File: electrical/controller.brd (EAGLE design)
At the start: 101.6 x 25.4 mm, 34 parts, among them IC1 MCP6232, IC2 LTC1661MSOP8, IC3 MCP6232, IC4 ICM7555, IC5 CD40109B, Q1 DMP3098, Q3 600mA/40V, U1 U3V16F15, U2 U3V16F15

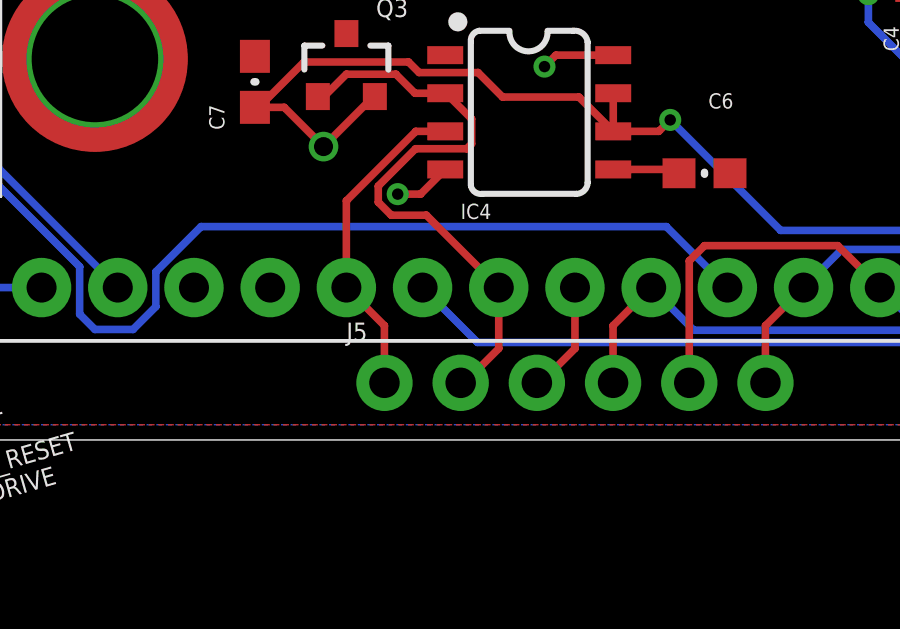
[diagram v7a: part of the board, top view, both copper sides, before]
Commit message: Some pin renaming to make things easier to understand...
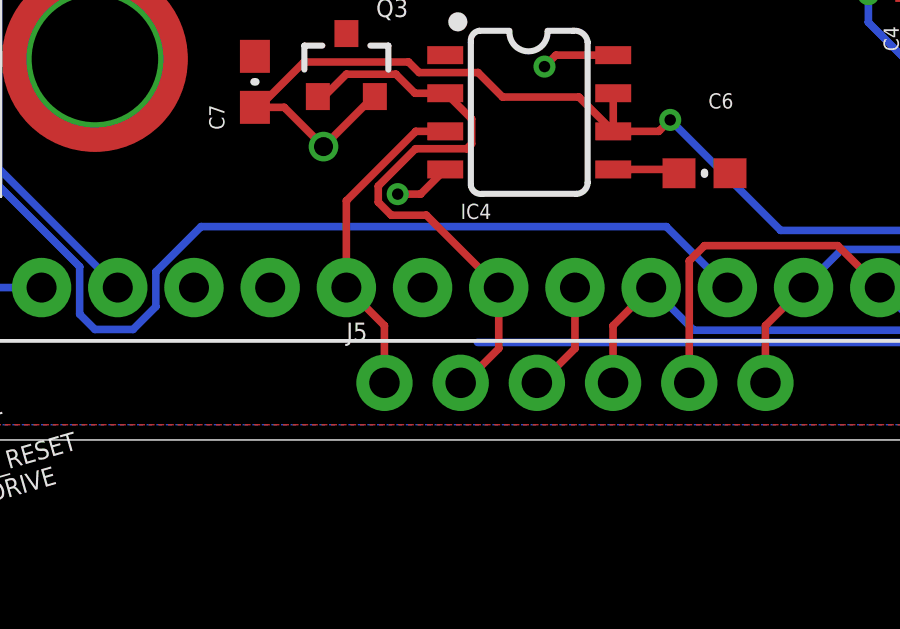
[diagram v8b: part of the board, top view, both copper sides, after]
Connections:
- net WAKE renamed BEMF_WAKE
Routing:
- net BEMF_WAKE: track 41.7 -> 39.1 mm
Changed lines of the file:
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@@
 <wire x1="60.10648125" y1="7.54651875" x2="60.10648125" y2="7.5644" width="0.254" layer="1"/>
-</signal>
-<signal name="WAKE">
-<contactref element="IC1" pad="7"/>
-<contactref element="UC1" pad="3"/>
-<wire x1="52.01" y1="6.985" x2="53.9082625" y2="6.985" width="0.254" layer="1"/>
-<wire x1="61.087" y1="1.905" x2="58.293" y2="4.699" width="0.254" layer="1"/>
-<wire x1="58.293" y1="4.699" x2="56.1942625" y2="4.699" width="0.254" layer="1"/>
-<wire x1="56.1942625" y1="4.699" x2="53.9082625" y2="6.985" width="0.254" layer="1"/>
-<contactref element="J4" pad="3"/>
-<wire x1="61.087" y1="1.905" x2="59.7408" y2="3.2512" width="0.254" layer="16"/>
-<wire x1="33.7058" y1="3.2512" x2="31.877" y2="5.08" width="0.254" layer="16"/>
-<wire x1="59.7408" y1="3.2512" x2="33.7058" y2="3.2512" width="0.254" layer="16"/>
 </signal>
 <signal name="DRIVE">
@@
 <wire x1="62.897" y1="9.798" x2="62.897" y2="10.598" width="0.254" layer="1"/>
 </signal>
+<signal name="BEMF_WAKE">
+<contactref element="UC1" pad="3"/>
+<contactref element="IC1" pad="7"/>
+<wire x1="52.01" y1="6.985" x2="53.9082625" y2="6.985" width="0.254" layer="1"/>
+<wire x1="61.087" y1="1.905" x2="58.293" y2="4.699" width="0.254" layer="1"/>
+<wire x1="58.293" y1="4.699" x2="56.1942625" y2="4.699" width="0.254" layer="1"/>
+<wire x1="56.1942625" y1="4.699" x2="53.9082625" y2="6.985" width="0.254" layer="1"/>
+<contactref element="J4" pad="3"/>
+<wire x1="61.087" y1="1.905" x2="59.7408" y2="3.2512" width="0.254" layer="16"/>
+<wire x1="59.7408" y1="3.2512" x2="33.7058" y2="3.2512" width="0.254" layer="16"/>
+<wire x1="33.7058" y1="3.2512" x2="31.877" y2="5.08" width="0" layer="19" extent="16-16"/>
+</signal>
 </signals>
